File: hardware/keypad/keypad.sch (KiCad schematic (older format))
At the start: 15 parts, among them SW1 SW_Push, SW2 SW_Push, SW3 SW_Push, SW4 SW_Push

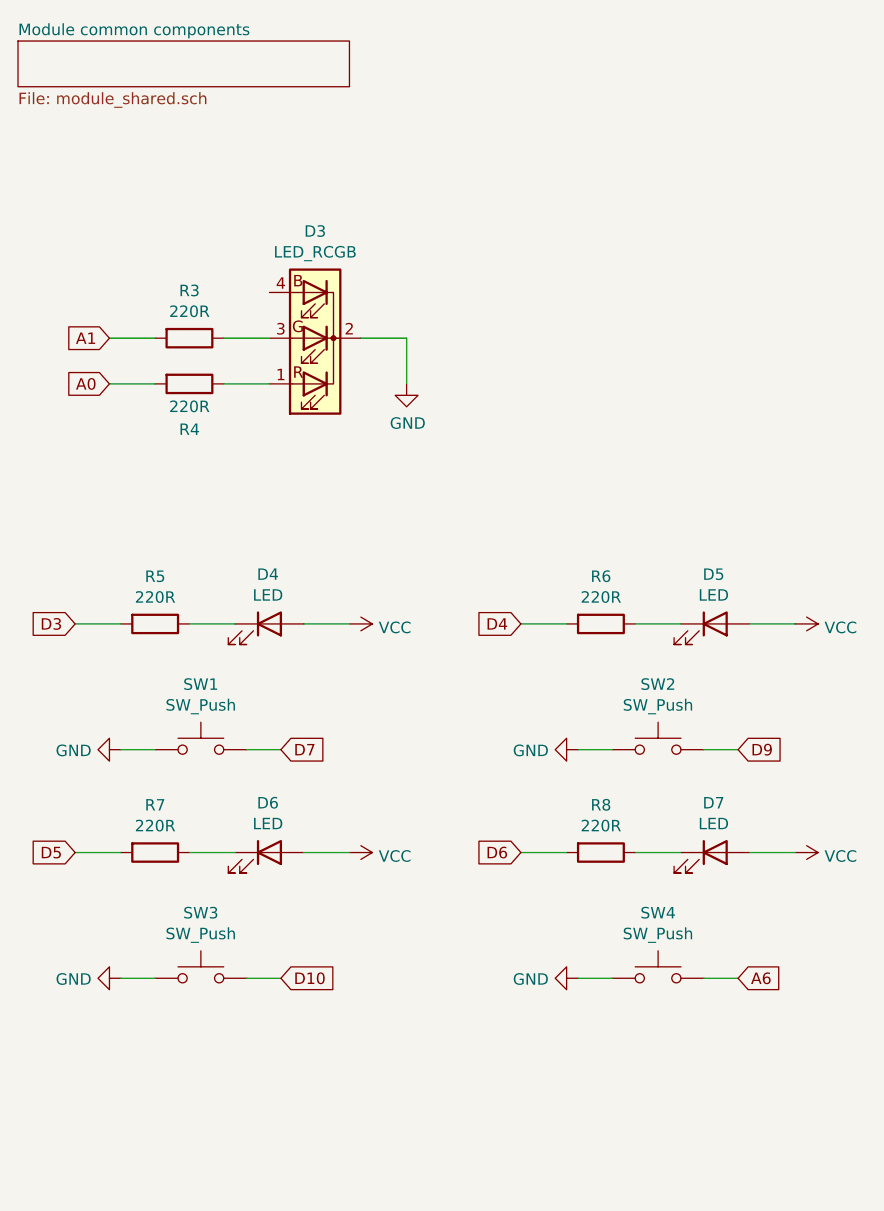
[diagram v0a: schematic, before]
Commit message: Keypad PCB: add debouncing caps
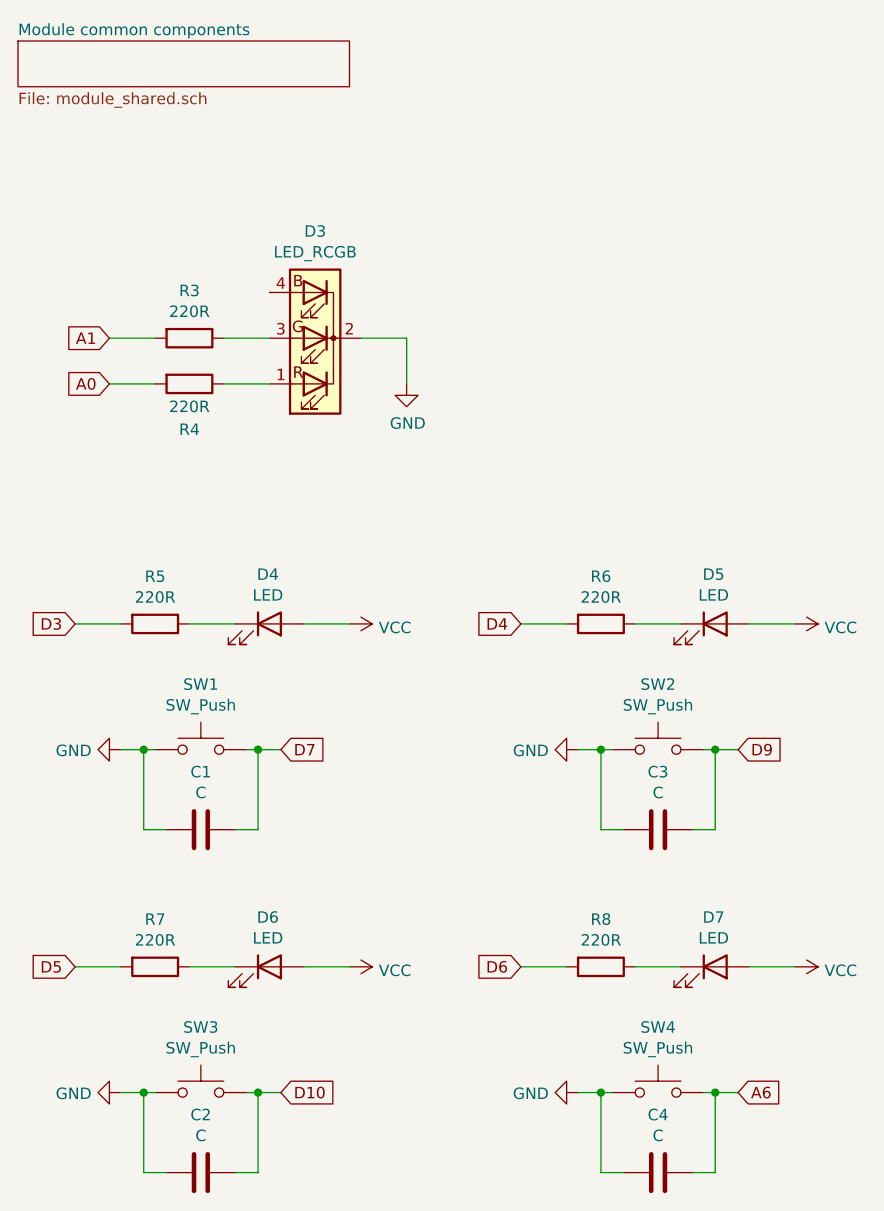
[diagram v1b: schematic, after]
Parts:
- added C1, C2, C3, C4: C, Capacitor_SMD:C_0805_2012Metric_Pad1.15x1.40mm_HandSolder, symbol Device:C
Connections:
- net A6: now also C4.1
- net D10: now also C2.1
- net D7: now also C1.1
- net D9: now also C3.1
- net GND: now also C1.2, C2.2, C3.2, C4.2
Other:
- moved on the sheet: D6, D7, R7, R8, SW3, SW4

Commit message: Keypad PCB: add holes for PCB-mounted switches
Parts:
- SW1, SW2, SW3, SW4: footprint Button_Switch_Keyboard:SW_Cherry_MX_1.00u_Plate -> Button_Switch_Keyboard:SW_Cherry_MX_1.00u_PCB
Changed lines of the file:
@@
 F 0 "SW1" H 1850 4235 50  0000 C CNN
 F 1 "SW_Push" H 1850 4144 50  0000 C CNN
-F 2 "Button_Switch_Keyboard:SW_Cherry_MX_1.00u_Plate" H 1850 4150 50  0001 C CNN
+F 2 "Button_Switch_Keyboard:SW_Cherry_MX_1.00u_PCB" H 1850 4150 50  0001 C CNN
 F 3 "~" H 1850 4150 50  0001 C CNN
 	1    1850 3950
@@
 F 0 "SW3" H 1850 5735 50  0000 C CNN
 F 1 "SW_Push" H 1850 5644 50  0000 C CNN
-F 2 "Button_Switch_Keyboard:SW_Cherry_MX_1.00u_Plate" H 1850 5650 50  0001 C CNN
+F 2 "Button_Switch_Keyboard:SW_Cherry_MX_1.00u_PCB" H 1850 5650 50  0001 C CNN
 F 3 "~" H 1850 5650 50  0001 C CNN
 	1    1850 5450
@@
 F 0 "SW2" H 3850 4235 50  0000 C CNN
 F 1 "SW_Push" H 3850 4144 50  0000 C CNN
-F 2 "Button_Switch_Keyboard:SW_Cherry_MX_1.00u_Plate" H 3850 4150 50  0001 C CNN
+F 2 "Button_Switch_Keyboard:SW_Cherry_MX_1.00u_PCB" H 3850 4150 50  0001 C CNN
 F 3 "~" H 3850 4150 50  0001 C CNN
 	1    3850 3950
@@
 F 0 "SW4" H 3850 5735 50  0000 C CNN
 F 1 "SW_Push" H 3850 5644 50  0000 C CNN
-F 2 "Button_Switch_Keyboard:SW_Cherry_MX_1.00u_Plate" H 3850 5650 50  0001 C CNN
+F 2 "Button_Switch_Keyboard:SW_Cherry_MX_1.00u_PCB" H 3850 5650 50  0001 C CNN
 F 3 "~" H 3850 5650 50  0001 C CNN
 	1    3850 5450

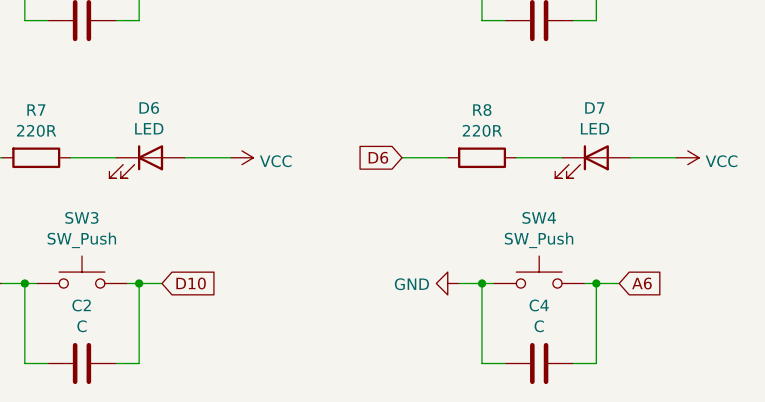
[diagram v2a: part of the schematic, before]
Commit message: Avoid using D10 (SPI SS) pin as input
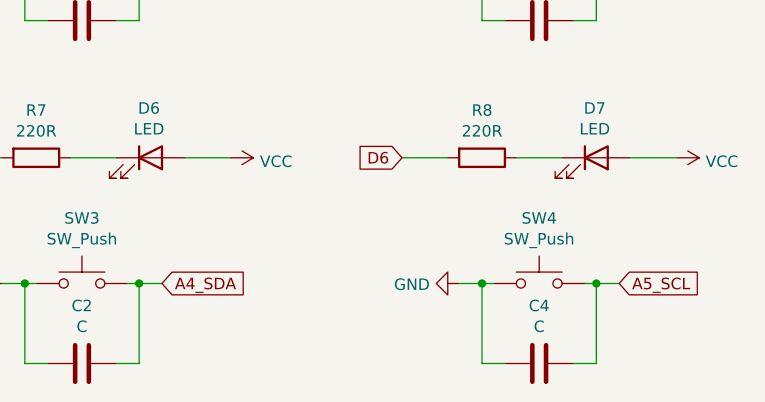
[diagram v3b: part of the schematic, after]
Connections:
- net A6 renamed A5_SCL
- net D10 renamed A4_SDA
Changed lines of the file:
@@
 	1500 5450 1600 5450
 Text GLabel 2200 5450 2    50   Input ~ 0
-D10
+A4_SDA
 Text GLabel 2200 3950 2    50   Input ~ 0
 D7
@@
 D9
 Text GLabel 4200 5450 2    50   Input ~ 0
-A6
+A5_SCL
 Wire Wire Line
 	4200 5450 4100 5450
